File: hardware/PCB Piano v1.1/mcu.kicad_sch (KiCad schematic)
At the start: 53 parts, among them J6 Micro_SD_Card, SW3 Reset Btn, SW4 Boot Select, SW5 Octave Select, SW6 Voice Select, U1 RP2040, U2 74LVC1G125, U7 W25Q128JVP, Y1 Crystal

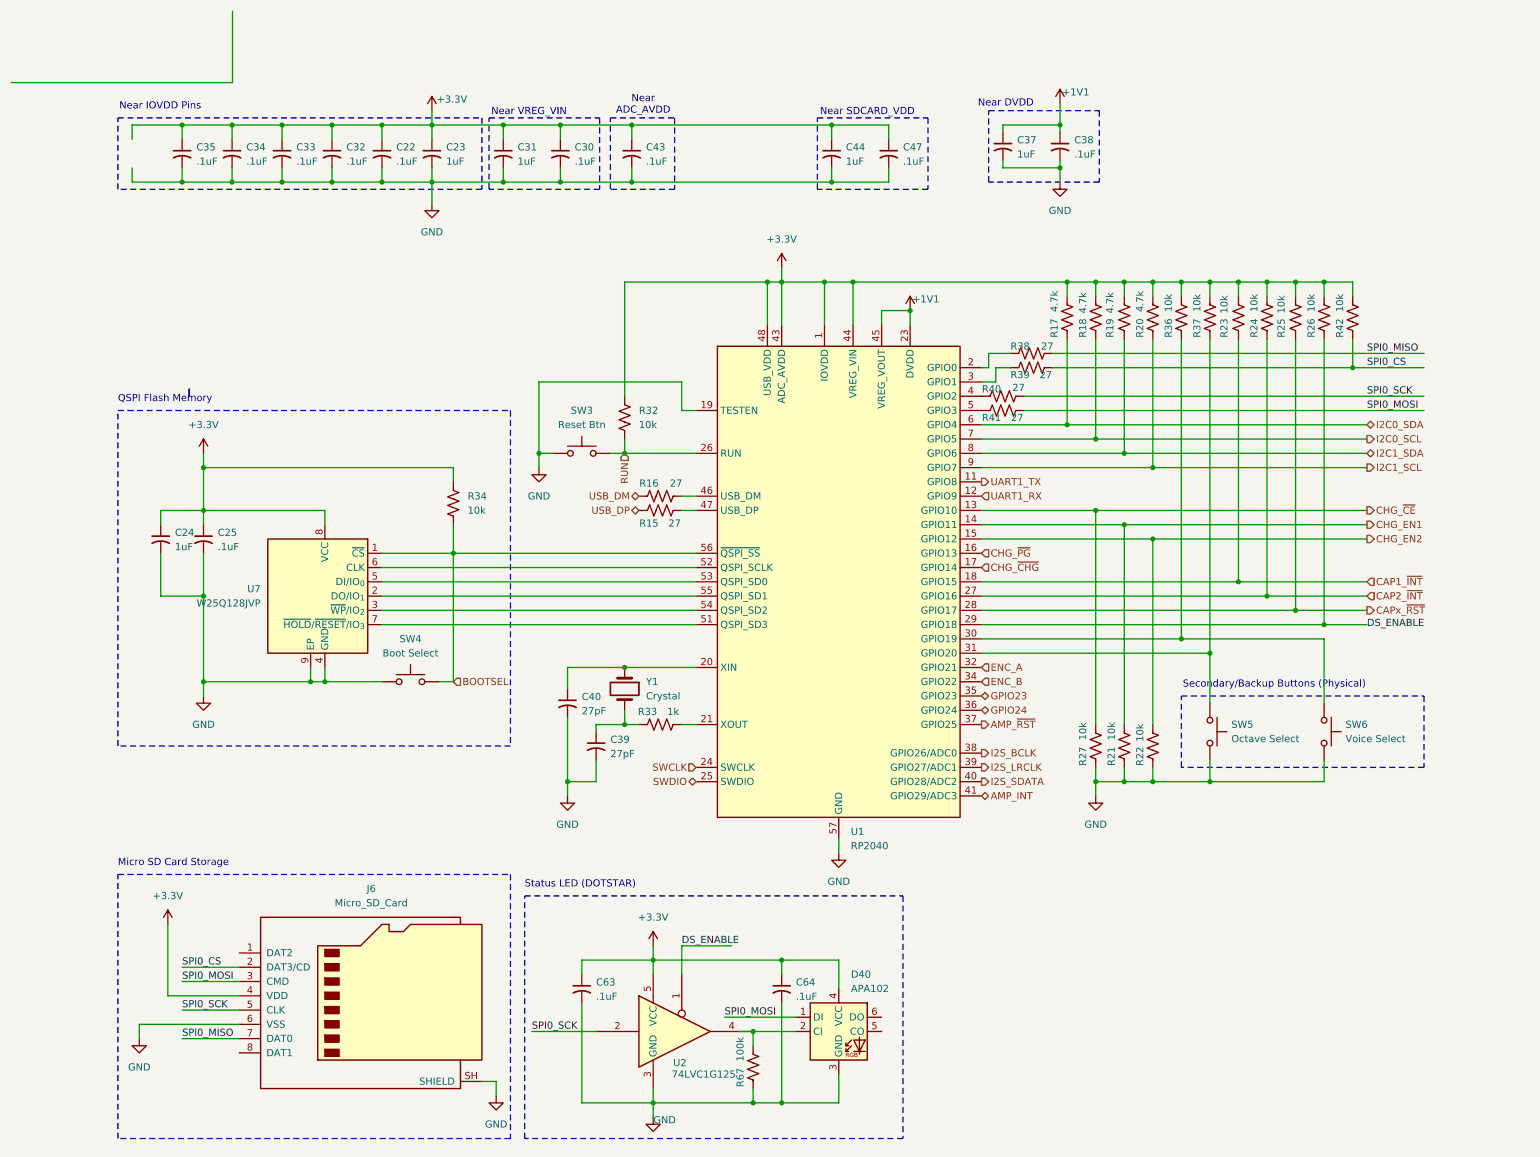
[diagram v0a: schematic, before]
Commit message: Development Phase - PCB Complete - ERC/DRC in progress
Development commit. PBC layout complete. ERC/DRC checks in progress. Swapped some connectors for JST connectors with Adafruit-style polarization.
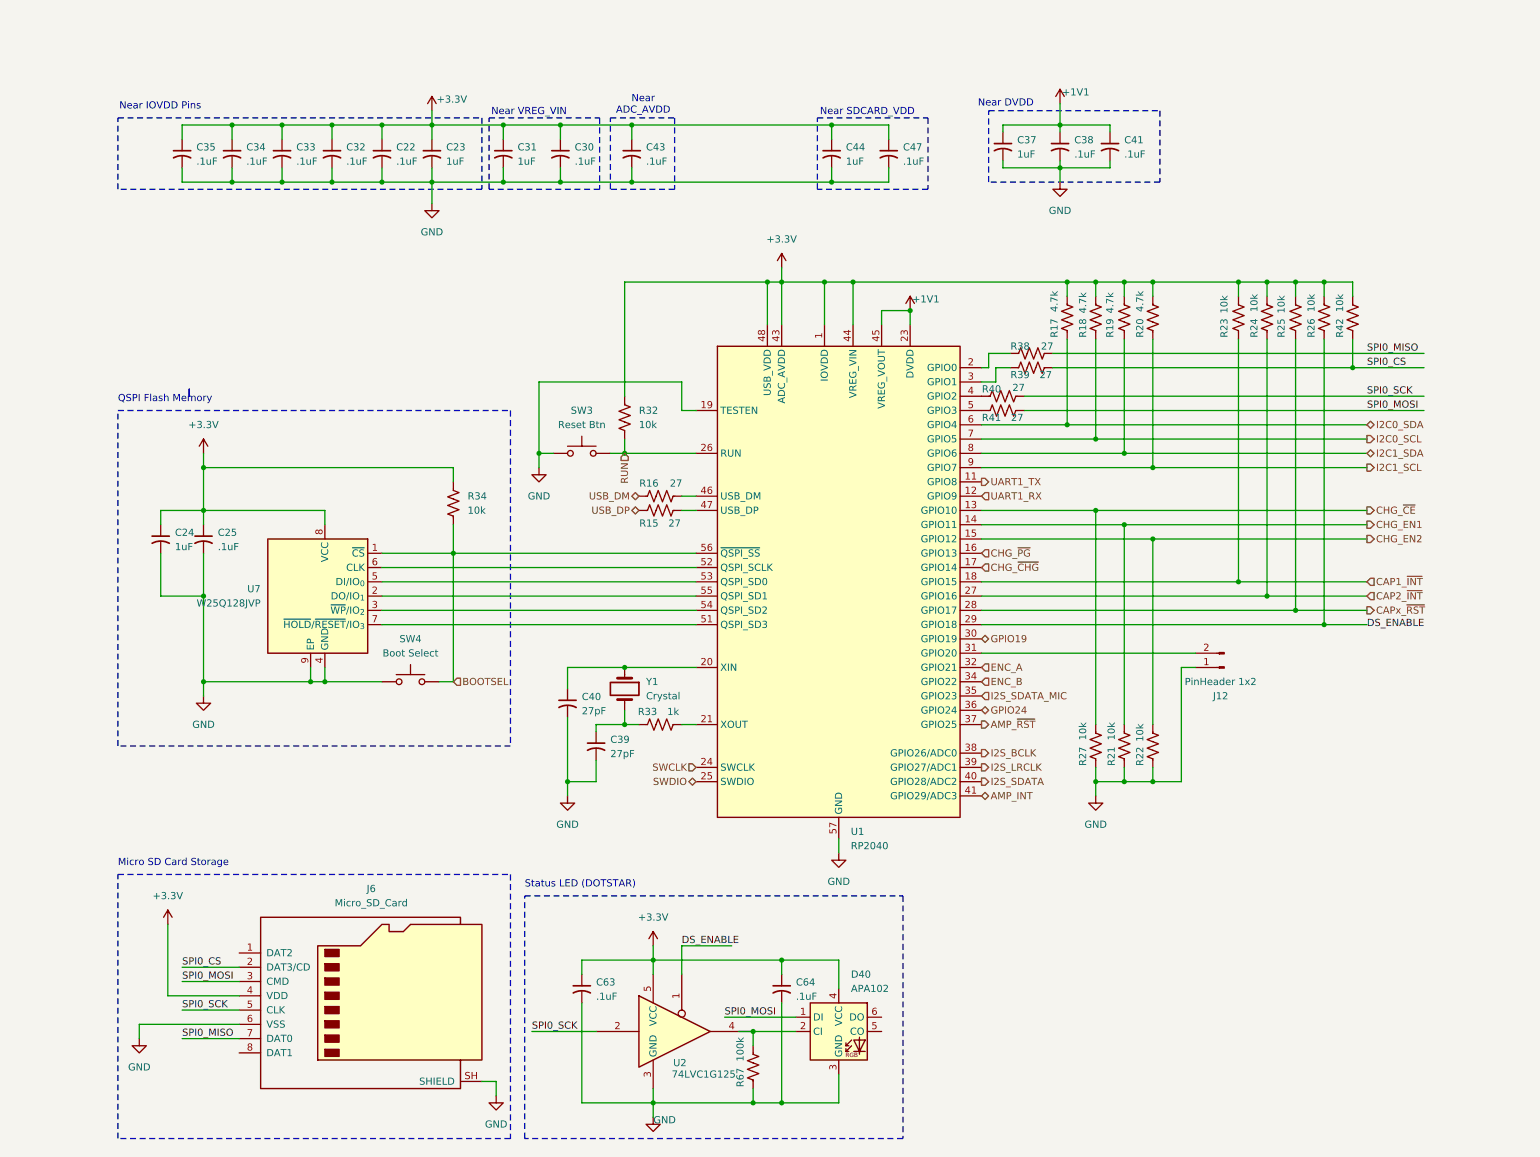
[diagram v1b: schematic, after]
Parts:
- removed R36, R37: 10k, Resistor_SMD:R_0603_1608Metric, symbol Device:R_US
- removed SW5: Octave Select, PCBPiano_Footprints:Button_Push_KMR6, symbol Switch:SW_Push
- removed SW6: Voice Select, PCBPiano_Footprints:Button_Push_KMR6, symbol Switch:SW_Push
- added C41: .1uF, Capacitor_SMD:C_0603_1608Metric, symbol Device:C_Small_US
- added J12: PinHeader 1x2, Connector_PinHeader_2.54mm:PinHeader_1x02_P2.54mm_Vertical_SMD_Pin1Left, symbol Connector:Conn_01x02_Pin
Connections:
- net +1V1: now also C41.1
- net GND: now also C41.2, J12.1 (Pin_1)
- net GPIO19: now reaches U1.30 (GPIO19)
- net at U1.31 (GPIO20): now also J12.2 (Pin_2)
- net GPIO23 renamed I2S_SDATA_MIC
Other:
- note removed: "Secondary/Backup Buttons (Physical)"

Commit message: Firmware architecture complete - PCB revision with new charger.
Firmware Architecture Complete

- Added MP2724 charger driver
- Added TLV320DAC3100 driver
- Added MTCH2120 touch driver
- Added PCA9685 driver
- Added DotStar driver
- Added rotary encoder driver
- Added touch and LED maps
- Added control/audio/voice managers
- Added audio command queue
- Added Core1 audio architecture
- Added status LED system
- Added LED animation framework

Changes hardware schematic and PCB to accommodate a newer-style USB-C sink battery charger chip and USB data MUX to protect MCU while powered off.
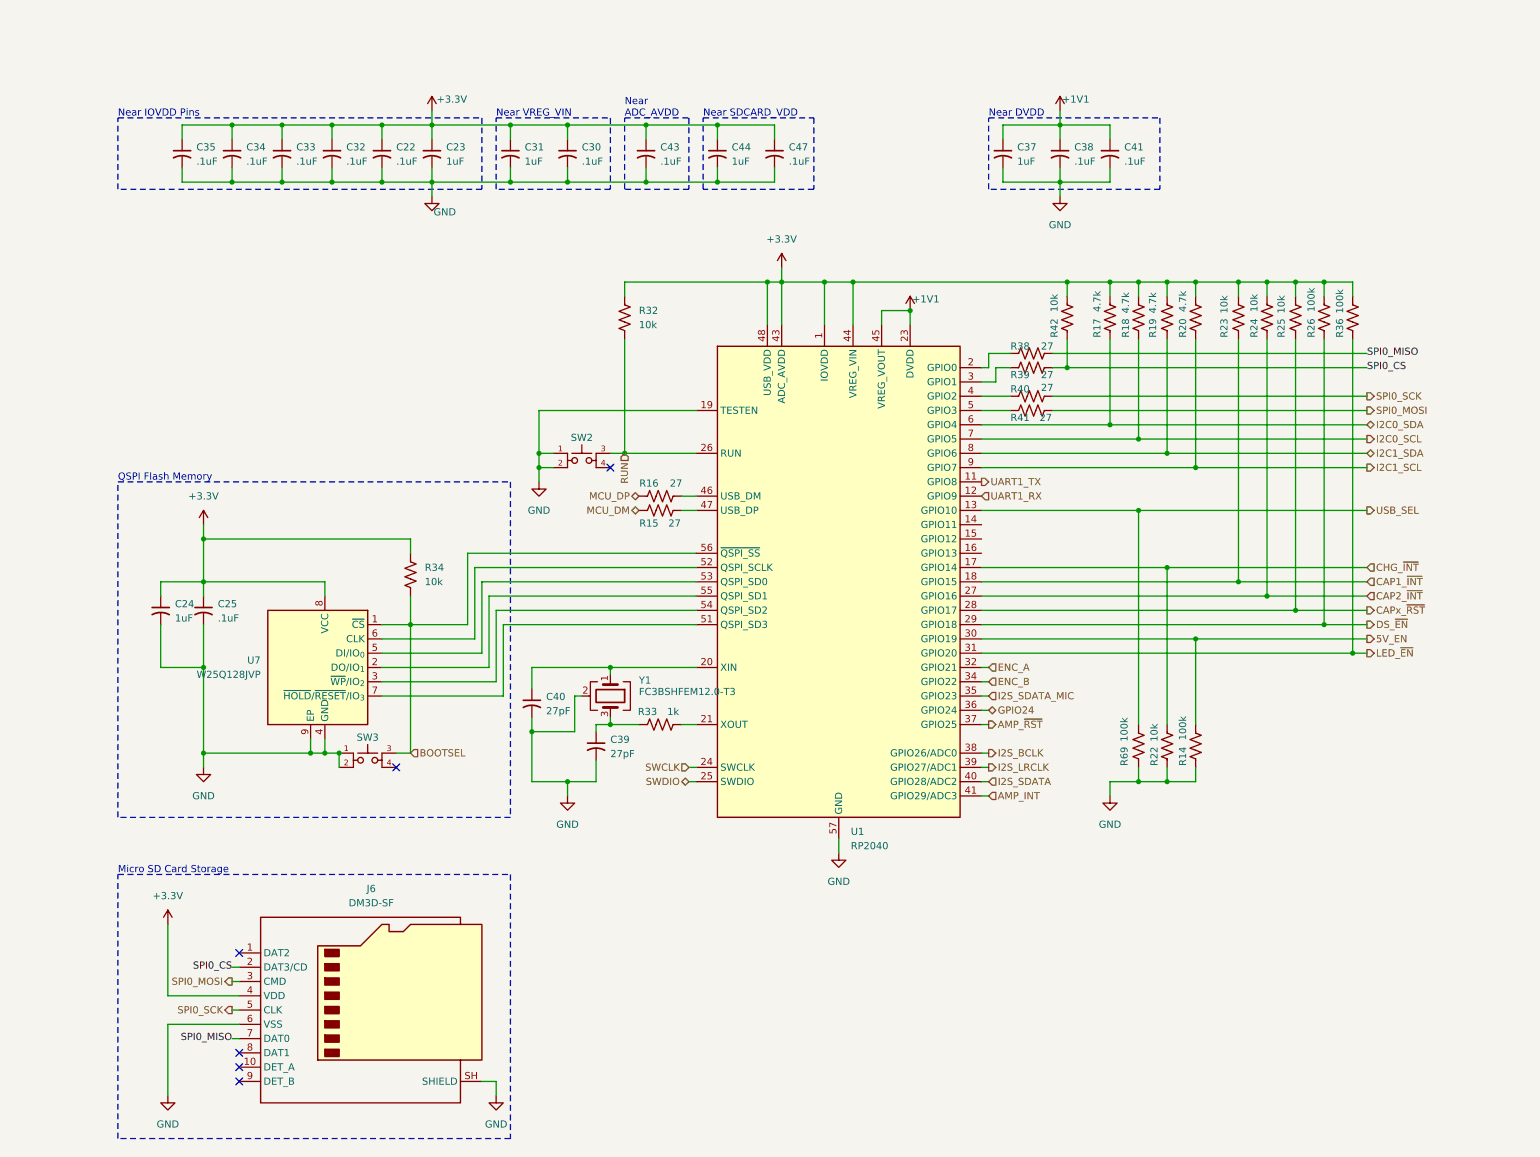
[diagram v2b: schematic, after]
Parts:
- removed C63, C64: .1uF, Capacitor_SMD:C_0603_1608Metric, symbol Device:C_Small_US
- removed D40: APA102, LED_SMD:LED_RGB_5050-6, symbol LED:APA102
- removed J12: PinHeader 1x2, Connector_PinHeader_2.54mm:PinHeader_1x02_P2.54mm_Vertical_SMD_Pin1Left, symbol Connector:Conn_01x02_Pin
- removed R21, R27: 10k, Resistor_SMD:R_0603_1608Metric, symbol Device:R_US
- removed R67: 100k, Resistor_SMD:R_0603_1608Metric, symbol Device:R_US
- removed SW3: Reset Btn, PCBPiano_Footprints:Button_Push_KMR6, symbol Switch:SW_Push
- removed SW4: Boot Select, PCBPiano_Footprints:Button_Push_KMR6, symbol Switch:SW_Push
- removed U2: 74LVC1G125, Package_TO_SOT_SMD:SOT-353_SC-70-5, symbol 74xGxx:74LVC1G125
- added R14, R36, R69: 100k, Resistor_SMD:R_0603_1608Metric, symbol Device:R_US
- added SW2, SW3: SWT0115-020025SSA_REVA, PCBPiano_Footprints:SW_SWT0115-020025SSA_REVA, symbol PCB_Piano_Symbols:SWT0115-020025SSA_REVA
- J6: value Micro_SD_Card -> DM3D-SF; footprint Connector_Card:microSD_HC_Hirose_DM3D-SF -> PCBPiano_Footprints:microSD_HC_Hirose_DM3D-SF; symbol Connector:Micro_SD_Card -> Connector:Micro_SD_Card_Det2
- R26: value 10k -> 100k
- Y1: value Crystal -> FC3BSHFEM12.0-T3; symbol Device:Crystal -> Device:Crystal_GND24
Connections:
- net +3.3V: now also R36.1
- net BOOTSEL: now also SW3.3
- net GND: now also Y1.2 (G), Y1.4 (G), R14.1, R69.2, SW2.1, SW2.2, SW3.1, SW3.2
- net RUN: now also SW2.3
- net LED_~{EN}: now reaches U1.31 (GPIO20)
- net LED_~{EN}: now also R36.2
- net at C39.1, R33.1: now also Y1.3; no longer Y1.2
- net CHG_EN1: no longer names the net of U1.14 (GPIO11)
- net CHG_EN2: no longer names the net of U1.15 (GPIO12)
- net CHG_EN2: no longer R22.1
- net CHG_~{CE} renamed USB_SEL
- net USB_SEL: now also R69.1
- net CHG_~{CHG} renamed CHG_~{INT}
- net CHG_~{INT}: now also R22.1
- net CHG_~{PG}: no longer names the net of U1.16 (GPIO13)
- net DS_ENABLE renamed DS_~{EN}
- net GPIO19 renamed 5V_EN
- net 5V_EN: now also R14.2
- net USB_DM renamed MCU_DP
- net USB_DP renamed MCU_DM
- no-connect marks 0 -> 6
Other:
- note removed: "Status LED (DOTSTAR)"
- moved on the sheet: C24, C25, C30, C31, C37, C38, C40, C41, C43, C44, C47, R17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

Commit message: PCB Finalized and Ordered. Firmware near completion.
PCB Finalized and Ordered. Final revisions included fixing bugs on some peripheral chips. Also added an RTC circuit after realizing the SD card could benefit from adding file timestamps.

Firmware near completion. Still need to finalize some SD card operations. Synth audio core is finished and all the board peripheral chip drivers were completed.
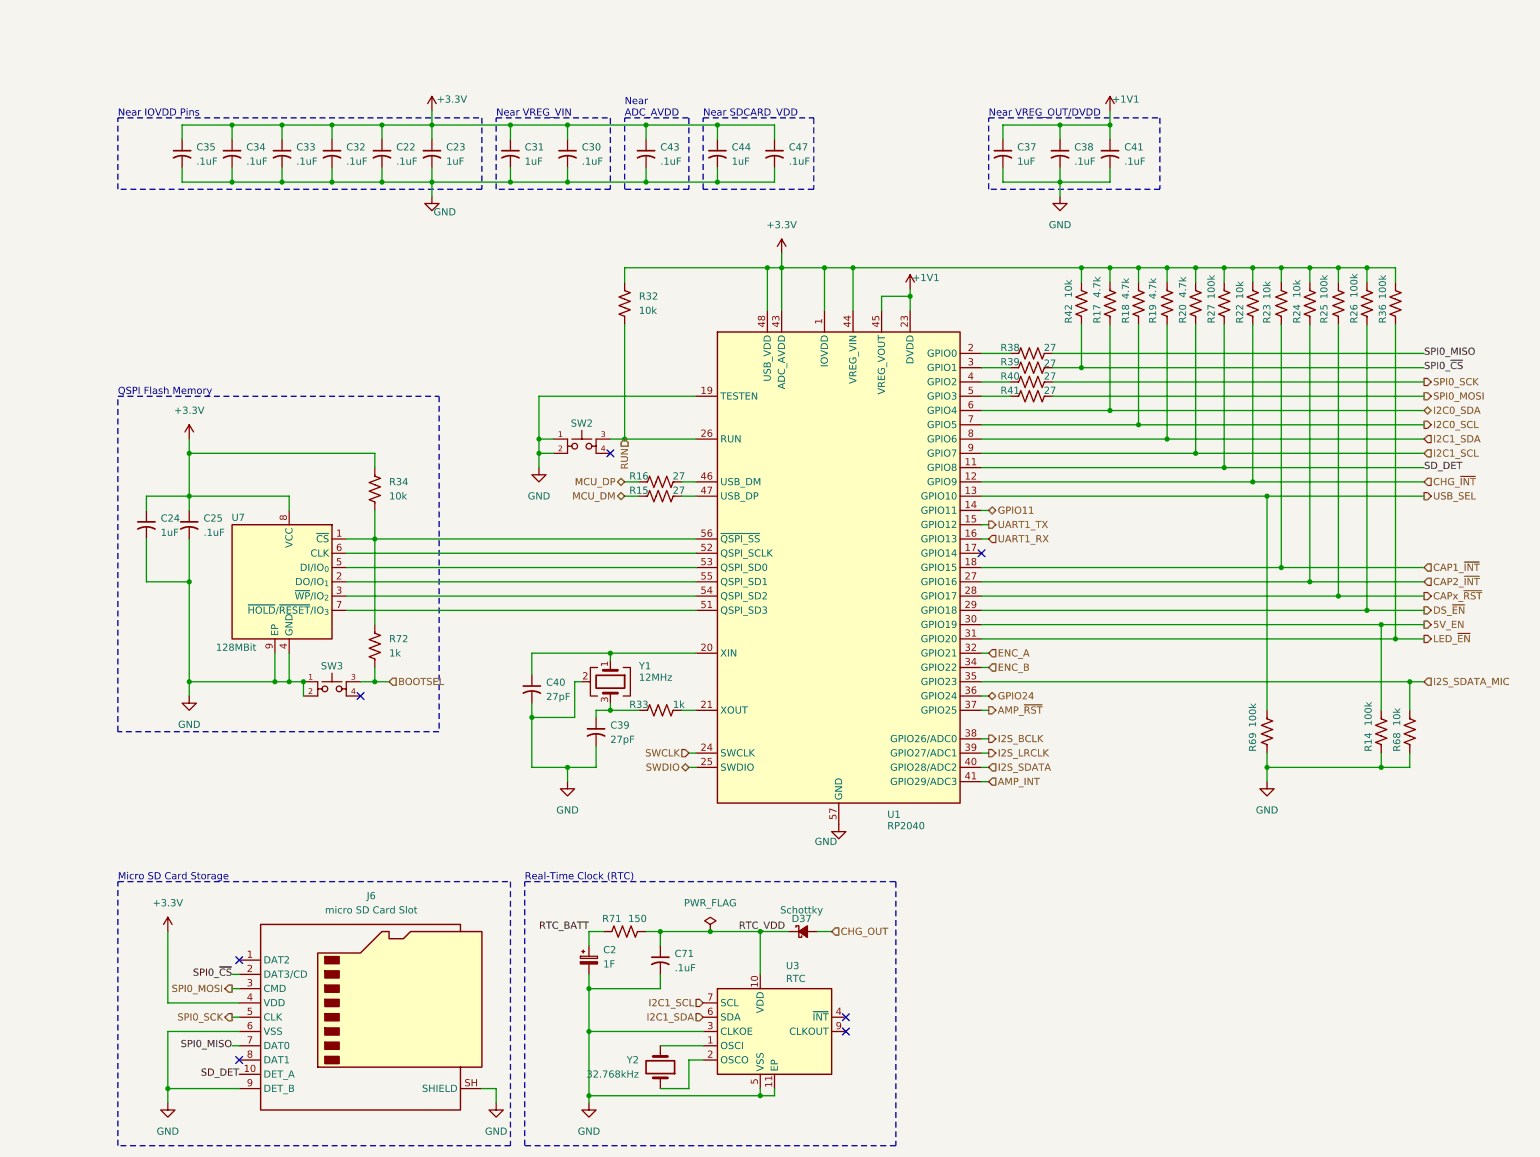
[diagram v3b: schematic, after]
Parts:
- added C2: 1F, PCBPiano_Footprints:SuperCap_HType_FoldedOutLegs, symbol Device:C_Polarized_Small
- added C71: .1uF, Capacitor_SMD:C_0603_1608Metric, symbol Device:C_Small_US
- added D37: Schottky, Diode_SMD:D_SOD-123, symbol Device:D_Schottky_Small_Filled
- added R27: 100k, Resistor_SMD:R_0603_1608Metric, symbol Device:R_US
- added R68: 10k, Resistor_SMD:R_0603_1608Metric, symbol Device:R_US
- added R71: 150, Resistor_SMD:R_1206_3216Metric, symbol Device:R_US
- added R72: 1k, Resistor_SMD:R_0603_1608Metric, symbol Device:R_US
- added U3: RTC, Package_DFN_QFN:DFN-10-1EP_2.6x2.6mm_P0.5mm_EP1.3x2.2mm, symbol PCB Piano Symbols:PCF85063ATL
- added Y2: 32.768kHz, PCBPiano_Footprints:Crystal_Kyocera_DT32_3.2x1.5mm, symbol Device:Crystal
- C22, C25, C30, C32, C33, C34, C35, C38, C41, C43, C47: DigiKey_Part_Number (none) -> 1276-1935-2-ND; Manufacturer Part Number (none) -> CL10B104KB8NNWC; Volt Rating (none) -> 10V
- C23, C24, C31, C37, C44: DigiKey_Part_Number (none) -> 1276-1184-1-ND; Manufacturer Part Number (none) -> CL10B105KA8NNNC; Volt Rating (none) -> 10V
- C39, C40: DigiKey_Part_Number (none) -> 478-KGM15ACG1E270JTCT-ND; Manufacturer Part Number (none) -> KGM15ACG1E270JT; Volt Rating (none) -> 10V
- J6: value DM3D-SF -> micro SD Card Slot; DigiKey_Part_Number (none) -> DM3D-SF; Manufacturer Part Number (none) -> DM3D-SF
- R25: value 10k -> 100k
- SW2, SW3: value SWT0115-020025SSA_REVA -> Pushbutton MO; DigiKey_Part_Number 2073-SWT0115-020025SSACT-ND -> SWT0115-020025SSA; Manufacturer Part Number (none) -> SWT0115-020025SSA
- U1: DigiKey_Part_Number (none) -> RP2040; Manufacturer Part Number (none) -> RP2040
- U7: value W25Q128JVP -> 128MBit; DigiKey_Part_Number (none) -> W25Q128JVP; Manufacturer Part Number (none) -> W25Q128JVP
- Y1: value FC3BSHFEM12.0-T3 -> 12MHz; DigiKey_Part_Number (none) -> FC3BSHFEM12.0-T3; Manufacturer Part Number (none) -> FC3BSHFEM12.0-T3
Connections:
- net +3.3V: now also R22.1, R27.1
- net BOOTSEL: now also R72.2; no longer R34.2, U1.56 (~{QSPI_SS}), U7.1 (~{CS})
- net CHG_~{INT}: now also R22.2, U1.12 (GPIO9); no longer R22.1, U1.17 (GPIO14)
- net GND: now also J6.9 (DET_B), C2.2, C71.2, R68.1, U3.11 (EP), U3.3 (CLKOE), U3.5 (VSS); no longer R22.2
- net I2C1_SCL: now also U3.7 (SCL)
- net I2C1_SDA: now also U3.6 (SDA)
- net I2S_SDATA_MIC: now also R68.2
- net UART1_RX: now also U1.16 (GPIO13); no longer U1.12 (GPIO9)
- net UART1_TX: now also U1.15 (GPIO12); no longer U1.11 (GPIO8)
- net SD_DET: now reaches J6.10 (DET_A)
- net SD_DET: now also U1.11 (GPIO8), R27.2
- net GPIO11: now reaches U1.14 (GPIO11)
- net SPI0_CS renamed SPI0_~{CS}
- new net: U3.2 (OSCO), Y2.1
- new net: U3.1 (OSCI), Y2.2
- new net: R34.2, R72.1, U1.56 (~{QSPI_SS}), U7.1 (~{CS})
- new net CHG_OUT: D37.2 (A)
- new net RTC_BATT: C2.1, R71.1
- new net RTC_VDD: C71.1, D37.1 (K), R71.2, U3.10 (VDD)
- no-connect marks 6 -> 7
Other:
- note added: "Near VREG_OUT/DVDD"
- note added: "Real-Time Clock (RTC)"
- note removed: "Near DVDD"
- moved on the sheet: C24, C25, C39, C40, J6, R14, R15, R16, R17, R18, R19, R20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
